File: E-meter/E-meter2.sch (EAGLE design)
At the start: 32 parts, among them IC1 LM324N, IC2 7805T

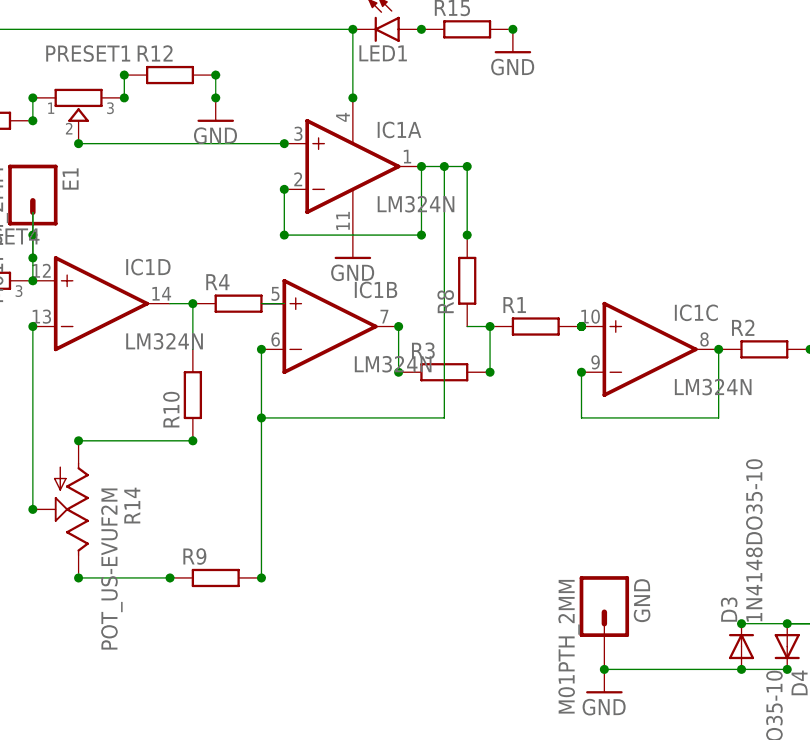
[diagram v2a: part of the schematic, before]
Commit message: last adjustments cleaning of last_fin not mirrored with Illustrator
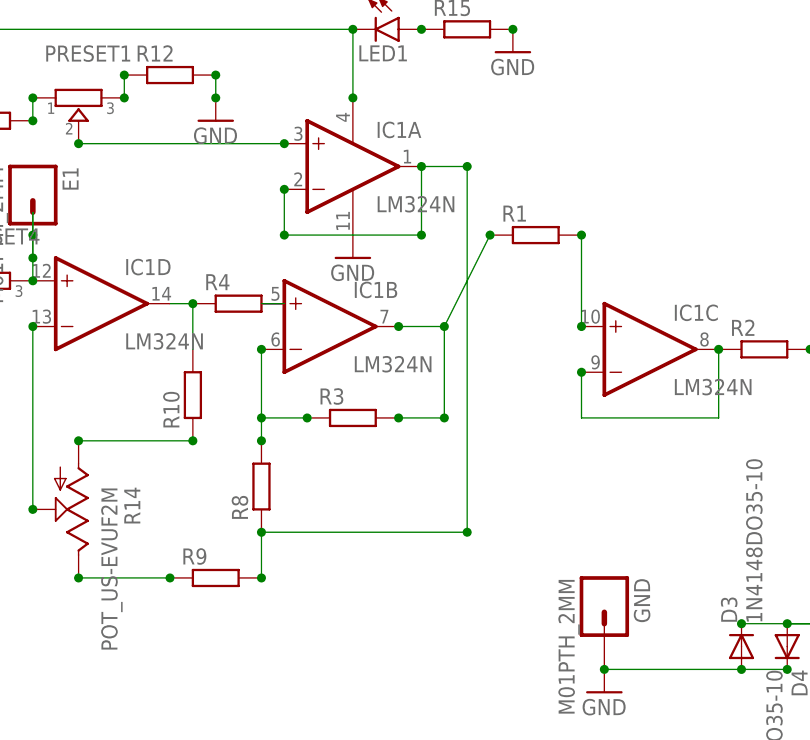
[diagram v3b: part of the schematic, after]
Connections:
- net N$22: now also IC1B.OUT; no longer R8.1
- net N$3: now also IC1B.-IN, R8.2; no longer IC1B.OUT
- net N$4: now also R8.1; no longer IC1B.-IN, R8.2
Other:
- moved on the sheet: R1, R3, R8
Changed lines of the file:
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@@
 <instance part="IC1" gate="C" x="101.6" y="38.1"/>
 <instance part="IC1" gate="D" x="40.64" y="43.18"/>
-<instance part="R1" gate="G$1" x="88.9" y="40.64"/>
+<instance part="R1" gate="G$1" x="88.9" y="50.8"/>
 <instance part="R2" gate="G$1" x="114.3" y="38.1"/>
-<instance part="R3" gate="G$1" x="78.74" y="35.56"/>
+<instance part="R3" gate="G$1" x="68.58" y="30.48"/>
 <instance part="R4" gate="G$1" x="55.88" y="43.18"/>
 <instance part="R5" gate="G$1" x="22.86" y="38.1"/>
 <instance part="R6" gate="G$1" x="22.86" y="33.02"/>
 <instance part="R7" gate="G$1" x="15.24" y="63.5"/>
-<instance part="R8" gate="G$1" x="81.28" y="45.72" rot="R90"/>
+<instance part="R8" gate="G$1" x="58.42" y="22.86" rot="R90"/>
 <instance part="R9" gate="G$1" x="53.34" y="12.7"/>
 <instance part="R10" gate="G$1" x="50.8" y="33.02" rot="R90"/>
@@
 <pinref part="R1" gate="G$1" pin="2"/>
 <pinref part="IC1" gate="C" pin="+IN"/>
+<wire x1="93.98" y1="50.8" x2="93.98" y2="40.64" width="0.1524" layer="91"/>
+<junction x="93.98" y="50.8"/>
 <junction x="93.98" y="40.64"/>
-<junction x="93.98" y="40.64"/>
-</segment>
-</net>
-<net name="N$3" class="0">
-<segment>
-<pinref part="IC1" gate="B" pin="OUT"/>
-<pinref part="R3" gate="G$1" pin="1"/>
-<wire x1="73.66" y1="35.56" x2="73.66" y2="40.64" width="0.1524" layer="91"/>
-<junction x="73.66" y="40.64"/>
-<junction x="73.66" y="35.56"/>
 </segment>
 </net>
 <net name="N$4" class="0">
 <segment>
-<pinref part="IC1" gate="B" pin="-IN"/>
-<junction x="58.42" y="38.1"/>
-<pinref part="R9" gate="G$1" pin="2"/>
-<wire x1="58.42" y1="12.7" x2="58.42" y2="30.48" width="0.1524" layer="91"/>
-<junction x="58.42" y="12.7"/>
-<wire x1="58.42" y1="38.1" x2="58.42" y2="30.48" width="0.1524" layer="91"/>
-<wire x1="81.28" y1="50.8" x2="81.28" y2="58.42" width="0.1524" layer="91"/>
 <pinref part="IC1" gate="A" pin="OUT"/>
-<wire x1="81.28" y1="58.42" x2="78.74" y2="58.42" width="0.1524" layer="91"/>
-<junction x="81.28" y="58.42"/>
 <junction x="76.2" y="58.42"/>
-<pinref part="R8" gate="G$1" pin="2"/>
-<wire x1="78.74" y1="58.42" x2="76.2" y2="58.42" width="0.1524" layer="91"/>
-<junction x="81.28" y="50.8"/>
+<wire x1="81.28" y1="58.42" x2="76.2" y2="58.42" width="0.1524" layer="91"/>
 <pinref part="IC1" gate="A" pin="-IN"/>
 <wire x1="60.96" y1="55.88" x2="60.96" y2="50.8" width="0.1524" layer="91"/>
@@
 <junction x="60.96" y="50.8"/>
 <junction x="60.96" y="55.88"/>
-<wire x1="58.42" y1="30.48" x2="78.74" y2="30.48" width="0.1524" layer="91"/>
-<wire x1="78.74" y1="30.48" x2="78.74" y2="58.42" width="0.1524" layer="91"/>
-<junction x="58.42" y="30.48"/>
-<junction x="78.74" y="58.42"/>
+<pinref part="R8" gate="G$1" pin="1"/>
+<pinref part="R9" gate="G$1" pin="2"/>
+<wire x1="58.42" y1="17.78" x2="58.42" y2="12.7" width="0.1524" layer="91"/>
+<junction x="58.42" y="12.7"/>
+<junction x="58.42" y="17.78"/>
+<wire x1="58.42" y1="17.78" x2="81.28" y2="17.78" width="0.1524" layer="91"/>
+<wire x1="81.28" y1="17.78" x2="81.28" y2="58.42" width="0.1524" layer="91"/>
+<junction x="81.28" y="58.42"/>
+<junction x="81.28" y="17.78"/>
 </segment>
 </net>
@@
 <net name="N$22" class="0">
 <segment>
-<pinref part="R8" gate="G$1" pin="1"/>
+<pinref part="IC1" gate="B" pin="OUT"/>
+<wire x1="78.74" y1="30.48" x2="73.66" y2="30.48" width="0.1524" layer="91"/>
+<pinref part="R3" gate="G$1" pin="2"/>
+<wire x1="73.66" y1="40.64" x2="78.74" y2="40.64" width="0.1524" layer="91"/>
+<wire x1="78.74" y1="40.64" x2="78.74" y2="30.48" width="0.1524" layer="91"/>
+<junction x="78.74" y="30.48"/>
+<junction x="73.66" y="40.64"/>
+<junction x="73.66" y="30.48"/>
 <pinref part="R1" gate="G$1" pin="1"/>
-<wire x1="81.28" y1="40.64" x2="83.82" y2="40.64" width="0.1524" layer="91"/>
-<junction x="83.82" y="40.64"/>
-<pinref part="R3" gate="G$1" pin="2"/>
-<wire x1="83.82" y1="40.64" x2="83.82" y2="35.56" width="0.1524" layer="91"/>
-<junction x="83.82" y="35.56"/>
+<wire x1="83.82" y1="50.8" x2="78.74" y2="40.64" width="0.1524" layer="91"/>
+<junction x="78.74" y="40.64"/>
+<junction x="83.82" y="50.8"/>
 </segment>
 </net>
@@
 </segment>
 </net>
+<net name="N$3" class="0">
+<segment>
+<pinref part="IC1" gate="B" pin="-IN"/>
+<junction x="58.42" y="38.1"/>
+<pinref part="R3" gate="G$1" pin="1"/>
+<wire x1="58.42" y1="30.48" x2="58.42" y2="38.1" width="0.1524" layer="91"/>
+<wire x1="63.5" y1="30.48" x2="58.42" y2="30.48" width="0.1524" layer="91"/>
+<junction x="63.5" y="30.48"/>
+<pinref part="R8" gate="G$1" pin="2"/>
+<wire x1="58.42" y1="30.48" x2="58.42" y2="27.94" width="0.1524" layer="91"/>
+<junction x="58.42" y="30.48"/>
+<junction x="58.42" y="27.94"/>
+</segment>
+</net>
